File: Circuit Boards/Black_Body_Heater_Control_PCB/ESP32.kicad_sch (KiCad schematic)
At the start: 17 parts, among them J3 USB_C_Receptacle_USB2.0_14P, J4 Conn_01x04_Pin, SW1 430471035826, SW2 430471035826, U1 ESP32-S3-WROOM-1-N8R8, U4 USBLC6-2SC6

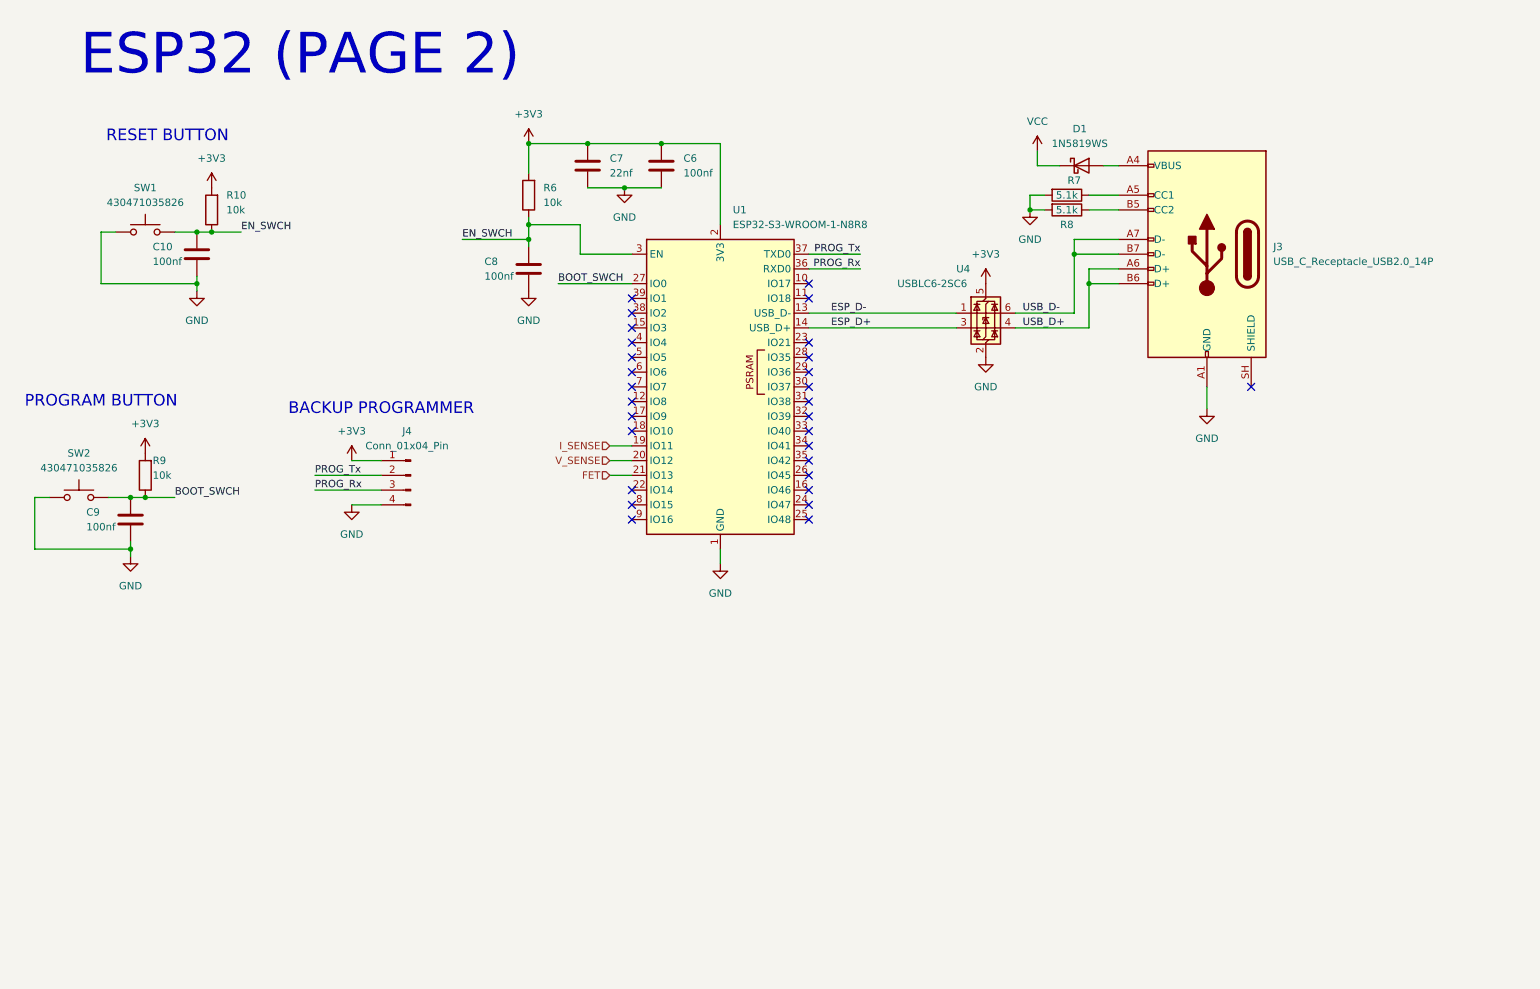
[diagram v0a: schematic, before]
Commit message: Heater PCB done (to review)
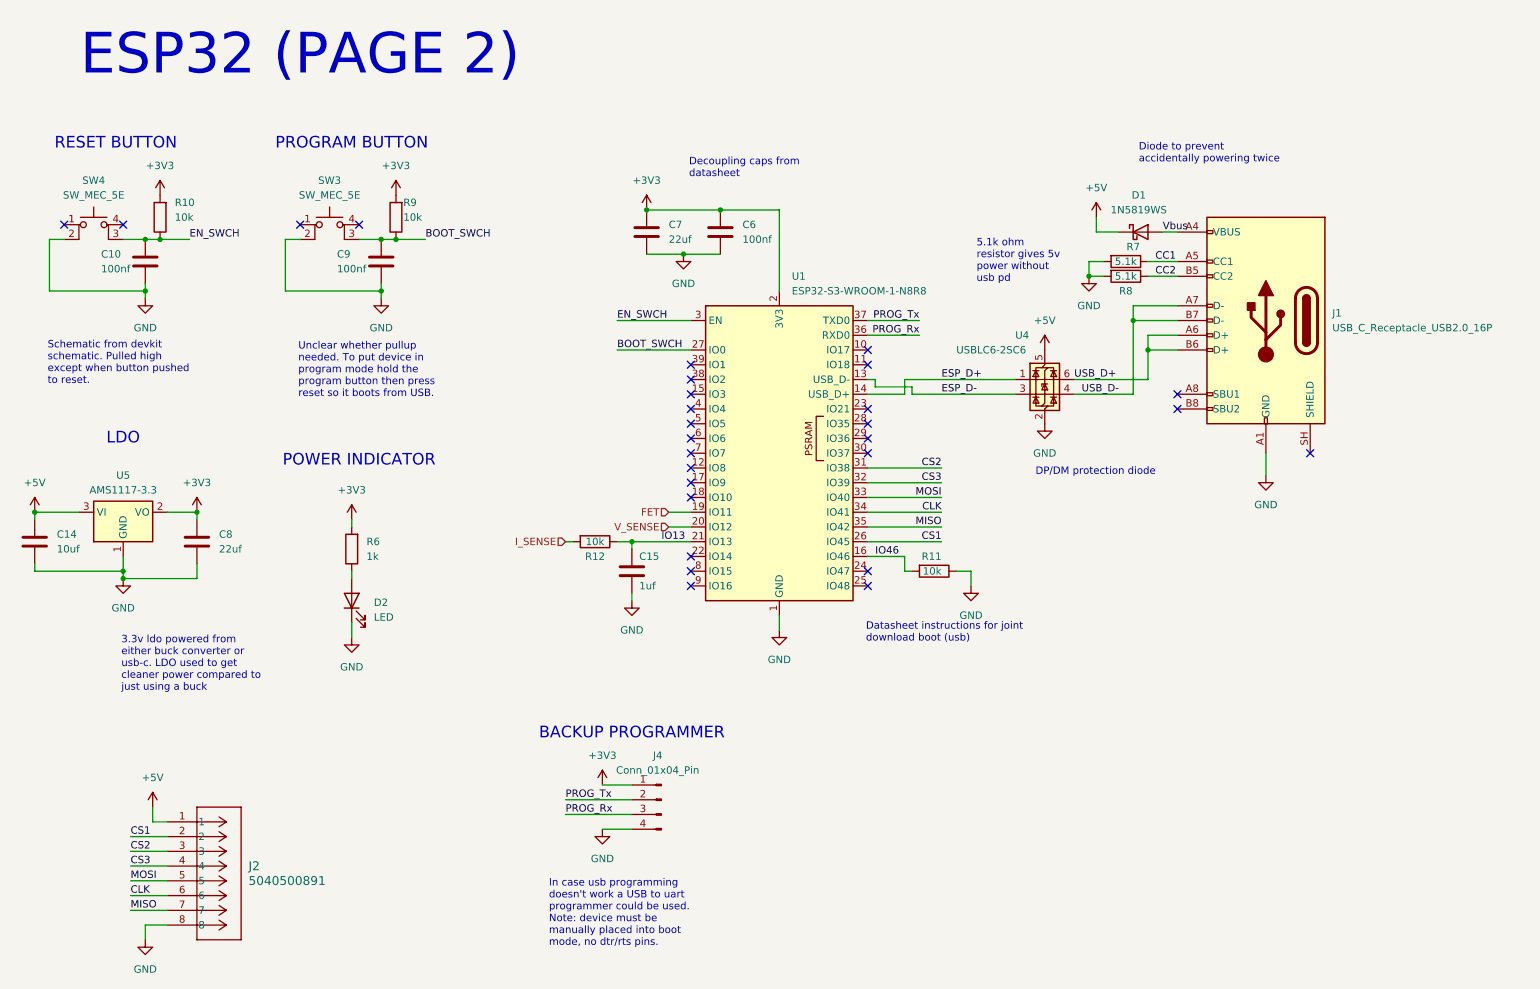
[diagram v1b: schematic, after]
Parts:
- removed J3: USB_C_Receptacle_USB2.0_14P, symbol Connector:USB_C_Receptacle_USB2.0_14P
- removed SW1, SW2: 430471035826, -switch:430471035826, symbol -switch:SW_Push
- added C14: 10uf, Capacitor_SMD:C_0603_1608Metric, symbol Device:C
- added C15: 1uf, Capacitor_SMD:C_0603_1608Metric, symbol Device:C
- added D2: LED, LED_SMD:LED_0603_1608Metric, symbol Device:LED
- added J1: USB_C_Receptacle_USB2.0_16P, -connector:UJ20-C-H-G-SMT-1-P16-TR, symbol Connector:USB_C_Receptacle_USB2.0_16P
- added J2: 5040500891, -connector:CONN_5040500891_MOL, symbol -connector:5040500891
- added R11, R12: 10k, Resistor_SMD:R_0603_1608Metric, symbol Device:R
- added SW3, SW4: SW_MEC_5E, -switch:430471035826, symbol Switch:SW_MEC_5E
- added U5: AMS1117-3.3, Package_TO_SOT_SMD:SOT-223-3_TabPin2, symbol Regulator_Linear:AMS1117-3.3
- C10, C6, C9: footprint (none) -> Capacitor_SMD:C_0603_1608Metric
- C7: value 22nf -> 22uf; footprint (none) -> Capacitor_SMD:C_0603_1608Metric
- C8: value 100nf -> 22uf; footprint (none) -> Capacitor_SMD:C_0603_1608Metric
- R10, R7, R8, R9: footprint (none) -> Resistor_SMD:R_0603_1608Metric
- R6: value 10k -> 1k; footprint (none) -> Resistor_SMD:R_0603_1608Metric
- U1: footprint RF_Module:ESP32-S3-WROOM-1 -> -mcu:ESP32-S3-WROOM-1
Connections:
- net +3V3: now also C8.1, U5.2 (VO); no longer U4.5 (VBUS)
- net BOOT_SWCH: now also SW3.3 (K)
- net EN_SWCH: now also SW4.3 (K); no longer C8.1, R6.1
- net ESP_D+: now also U4.1 (I/O1); no longer U4.3 (I/O2)
- net ESP_D-: now also U4.3 (I/O2); no longer U4.1 (I/O1)
- net FET: now also U1.19 (IO11); no longer U1.21 (IO13)
- net GND: now also C14.2, C15.2, D2.1 (K), J1.A1 (GND), J1.A12 (GND), J1.B1 (GND), J1.B12 (GND), J2.8, R11.1, SW3.2, SW4.2, U5.1 (GND)
- net I_SENSE: now also R12.2; no longer U1.19 (IO11)
- net USB_D+: now also U4.6 (I/O1), J1.A6 (D+), J1.B6 (D+); no longer U4.4 (I/O2)
- net USB_D-: now also U4.4 (I/O2), J1.A7 (D-), J1.B7 (D-); no longer U4.6 (I/O1)
- net Vbus: now reaches D1.2 (A)
- net Vbus: now also J1.A4 (VBUS), J1.A9 (VBUS), J1.B4 (VBUS), J1.B9 (VBUS)
- net IO46: now reaches U1.16 (IO46)
- net IO46: now also R11.2
- net CS1: now reaches U1.26 (IO45)
- net CS1: now also J2.2
- net CS2: now reaches U1.31 (IO38)
- net CS2: now also J2.3
- net CS3: now reaches U1.32 (IO39)
- net CS3: now also J2.4
- net MOSI: now reaches U1.33 (IO40)
- net MOSI: now also J2.5
- net CLK: now reaches U1.34 (IO41)
- net CLK: now also J2.6
- net MISO: now reaches U1.35 (IO42)
- net MISO: now also J2.7
- net CC1: now reaches R7.1
- net CC1: now also J1.A5 (CC1)
- net CC2: now reaches R8.1
- net CC2: now also J1.B5 (CC2)
- net VCC renamed +5V
- net +5V: now also U4.5 (VBUS), C14.1, J2.1, U5.3 (VI)
- new net: D2.2 (A), R6.1
- new net IO13: C15.1, R12.1, U1.21 (IO13)
- no-connect marks 29 -> 28
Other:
- note added: "LDO"
- note added: "POWER INDICATOR"
- moved on the sheet: C10, C6, C7, C9, D1, J4, R10, R7, R8, R9, U1

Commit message: Temp sensor schematic done
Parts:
- D2: value LED -> RED
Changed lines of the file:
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@@
 			)
 		)
-		(property "Value" "LED"
+		(property "Value" "RED"
 			(at 90.17 123.5074 90)
 			(show_name no)

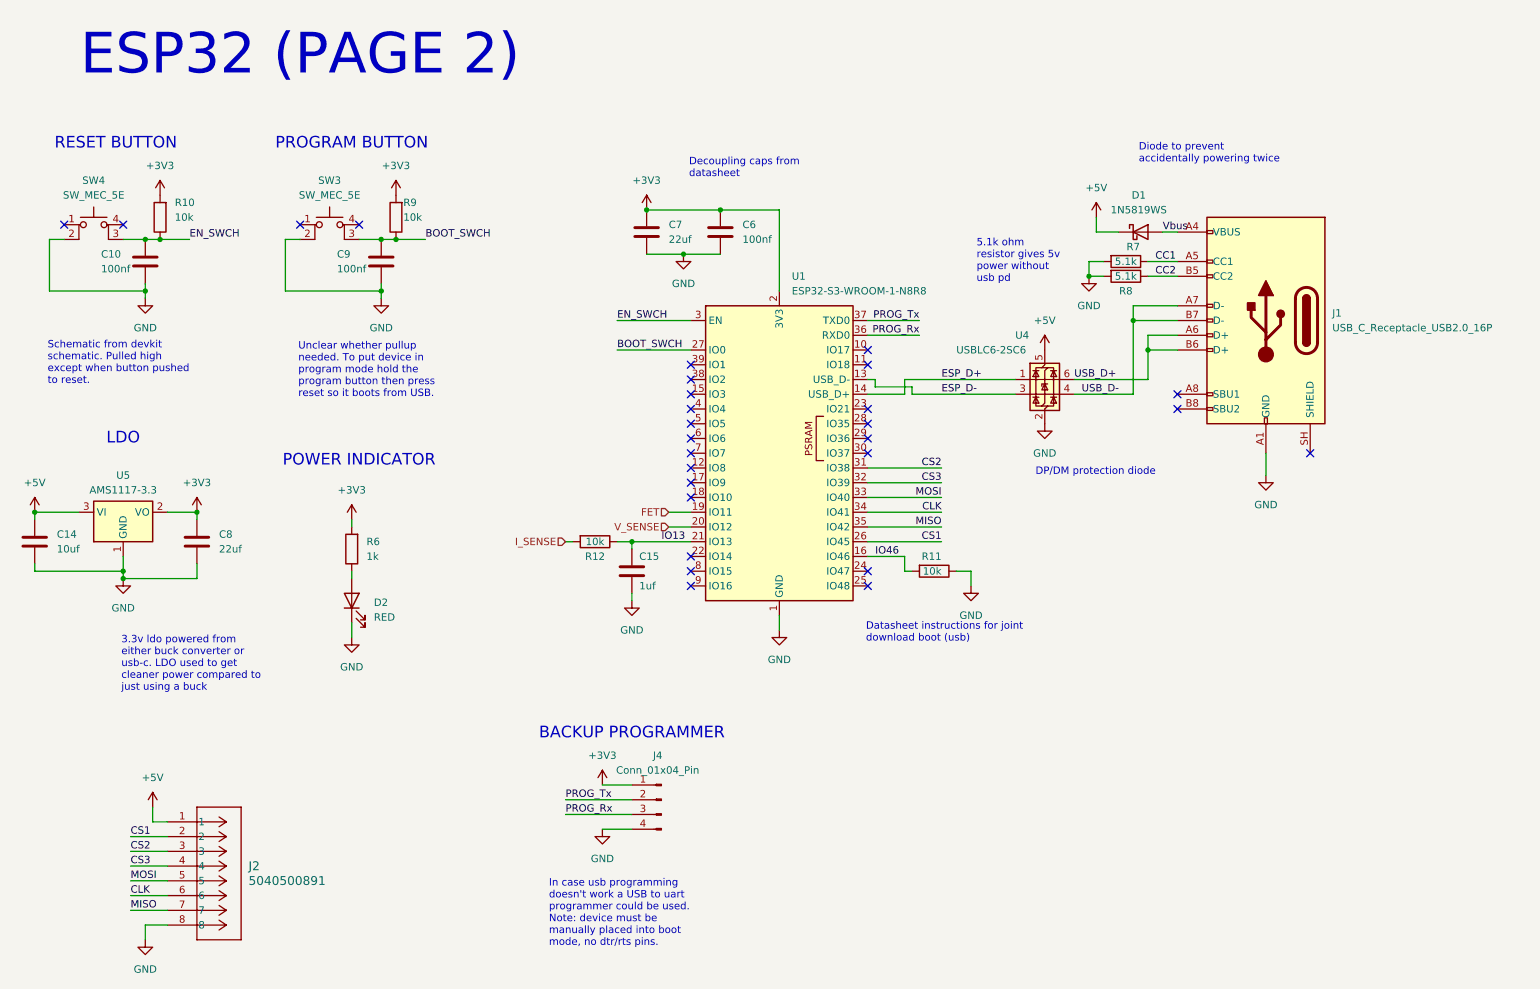
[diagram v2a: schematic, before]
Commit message: Heater switched from pwm to vccs
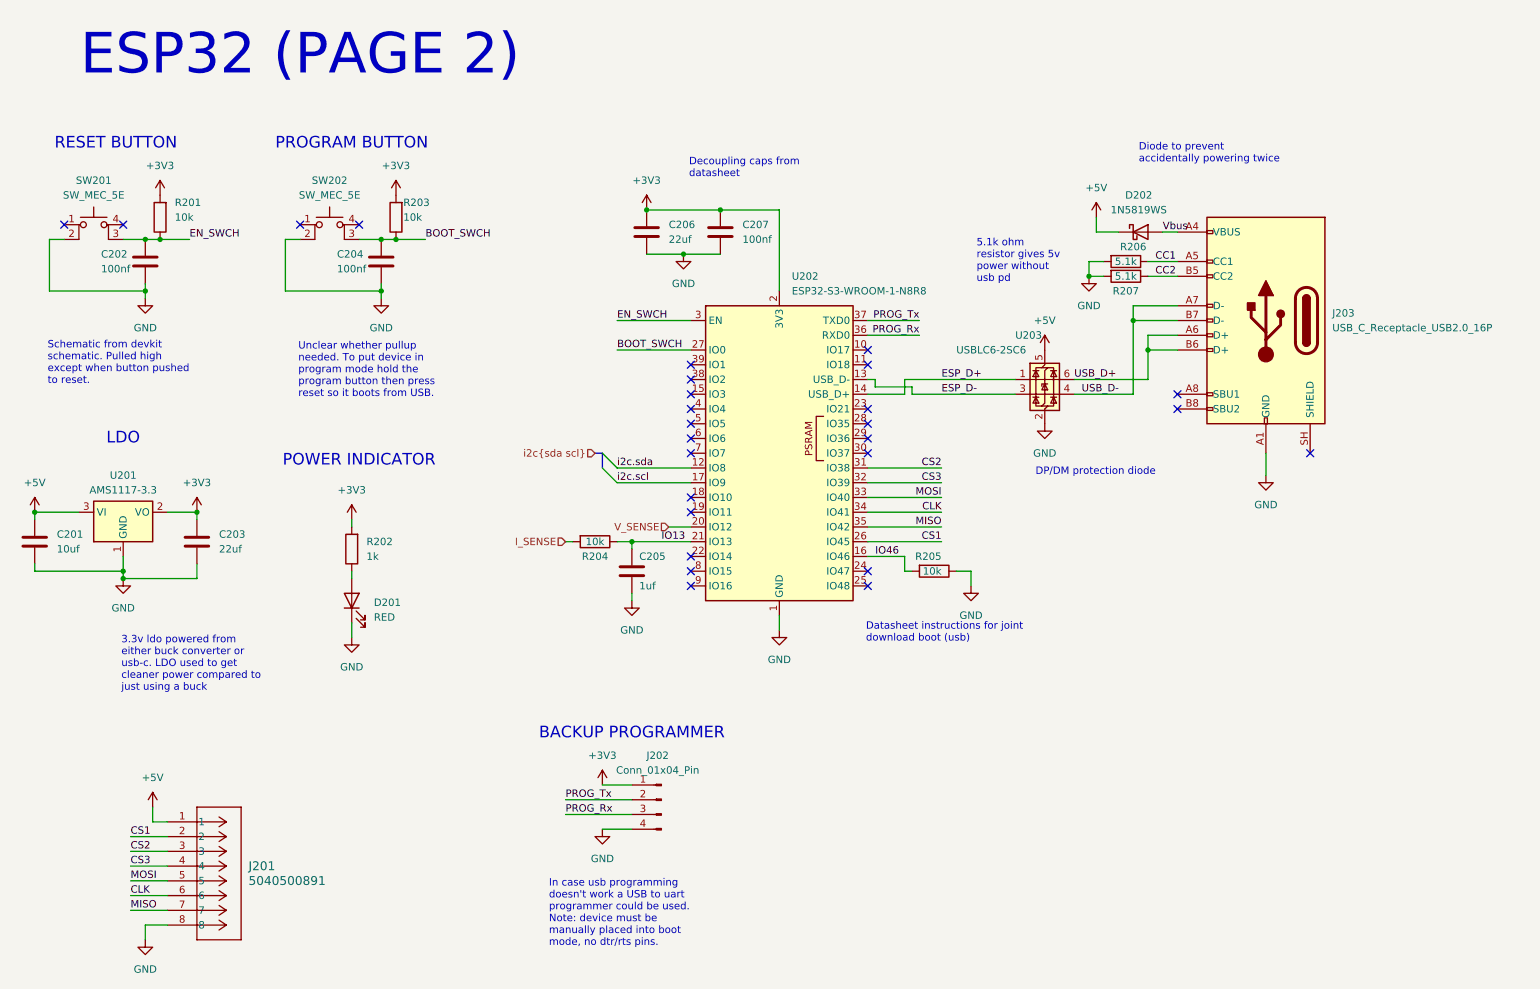
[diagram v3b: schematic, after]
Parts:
- renumbered C14 to C201, C10 to C202, C8 to C203, C9 to C204, C15 to C205, C7 to C206, C6 to C207, D2 to D201, D1 to D202, J2 to J201, J4 to J202, J1 to J203, R10 to R201, R6 to R202, R9 to R203, R12 to R204, R11 to R205, R7 to R206, R8 to R207, SW4 to SW201, SW3 to SW202, U5 to U201, U1 to U202, U4 to U203
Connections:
- net i2c.sda: now reaches U202.12 (IO8)
- net i2c.scl: now reaches U202.17 (IO9)
- net FET: no longer names the net of U202.19 (IO11)
- no-connect marks 28 -> 27

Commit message: heater ready to order
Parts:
- D202: MPN (none) -> 1N5819WS
- J201: MPN (none) -> 5040500891
- J202: now not fitted; now left out of the parts list
- J203: MPN (none) -> UJ20-C-H-G-SMT-1-P16-TR
- SW201, SW202: MPN (none) -> SW_MEC_5E
- U201: MPN (none) -> AMS1117-3.3
- U202: MPN (none) -> ESP32-S3-WROOM-1-N8R8
- U203: MPN (none) -> USBLC6-2SC6
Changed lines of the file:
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@@
 			)
 		)
+		(property "MPN" "SW_MEC_5E"
+			(at 41.91 58.42 0)
+			(hide yes)
+			(show_name no)
+			(do_not_autoplace no)
+			(effects
+				(font
+					(size 1.27 1.27)
+				)
+			)
+		)
 		(pin "4"
 		)
@@
 			)
 		)
+		(property "MPN" "USBLC6-2SC6"
+			(at 205.74 82.55 0)
+			(hide yes)
+			(show_name no)
+			(do_not_autoplace no)
+			(effects
+				(font
+					(size 1.27 1.27)
+				)
+			)
+		)
 		(pin "4"
 		)
@@
 	)
 	(symbol
+		(lib_id "Switch:SW_MEC_5E")
+		(at 82.55 58.42 0)
+		(unit 1)
+		(body_style 1)
+		(exclude_from_sim no)
+		(in_bom yes)
+		(on_board yes)
+		(in_pos_files yes)
+		(dnp no)
+		(fields_autoplaced yes)
+		(property "Reference" "SW202"
+			(at 82.55 48.26 0)
+			(show_name no)
+			(do_not_autoplace no)
+			(effects
+				(font
+					(size 1.27 1.27)
+				)
+			)
+		)
+		(property "Value" "SW_MEC_5E"
+			(at 82.55 50.8 0)
+			(show_name no)
+			(do_not_autoplace no)
+			(effects
+				(font
+					(size 1.27 1.27)
+				)
+			)
+		)
+		(property "Footprint" "-switch:430471035826"
+			(at 82.55 50.8 0)
+			(hide yes)
+			(show_name no)
+			(do_not_autoplace no)
+			(effects
+				(font
+					(size 1.27 1.27)
+				)
+			)
+		)
+		(property "Datasheet" "https://www.apem.com/medias/download/MEC_switches_serie_MULTIMEC5E.pdf"
+			(at 82.55 50.8 0)
+			(hide yes)
+			(show_name no)
+			(do_not_autoplace no)
+			(effects
+				(font
+					(size 1.27 1.27)
+				)
+			)
+		)
+		(property "Description" "MEC 5E single pole normally-open tactile switch"
+			(at 82.55 58.42 0)
+			(hide yes)
+			(show_name no)
+			(do_not_autoplace no)
+			(effects
+				(font
+					(size 1.27 1.27)
+				)
+			)
+		)
+		(property "MPN" "SW_MEC_5E"
+			(at 82.55 58.42 0)
+			(hide yes)
+			(show_name no)
+			(do_not_autoplace no)
+			(effects
+				(font
+					(size 1.27 1.27)
+				)
+			)
+		)
+		(pin "4"
+		)
+		(pin "3"
+		)
+		(pin "2"
+		)
+		(pin "1"
+		)
+		(instances
+			(project "Black_Body_Heater_Control"
+				(path "/f3dd8e24-b1a1-45ed-a541-b7ae36b7e8e0/81e90e05-0519-429e-85ab-ffede3727917"
+					(reference "SW202")
+					(unit 1)
+				)
+			)
+		)
+	)
+	(symbol
 		(lib_id "Diode:1N5819WS")
 		(at 222.25 57.15 0)
@@
 			)
 		)
+		(property "MPN" "1N5819WS"
+			(at 222.25 57.15 0)
+			(hide yes)
+			(show_name no)
+			(do_not_autoplace no)
+			(effects
+				(font
+					(size 1.27 1.27)
+				)
+			)
+		)
 		(pin "1"
 		)
@@
 			)
 		)
+		(property "MPN" "ESP32-S3-WROOM-1-N8R8"
+			(at 160.02 95.25 0)
+			(hide yes)
+			(show_name no)
+			(do_not_autoplace no)
+			(effects
+				(font
+					(size 1.27 1.27)
+				)
+			)
+		)
 		(pin "1"
 		)
@@
 			)
 		)
+		(property "MPN" "UJ20-C-H-G-SMT-1-P16-TR"
+			(at 243.84 72.39 0)
+			(hide yes)
+			(show_name no)
+			(do_not_autoplace no)
+			(effects
+				(font
+					(size 1.27 1.27)
+				)
+			)
+		)
 		(pin "A4"
 		)
@@
 			)
 		)
+		(property "MPN" "5040500891"
+			(at 54.61 158.75 0)
+			(hide yes)
+			(show_name yes)
+			(do_not_autoplace no)
+			(effects
+				(font
+					(size 1.27 1.27)
+				)
+				(justify bottom)
+			)
+		)
 		(pin "4"
 		)
@@
 	)
 	(symbol
-		(lib_id "Switch:SW_MEC_5E")
-		(at 82.55 58.42 0)
-		(unit 1)
-		(body_style 1)
-		(exclude_from_sim no)
-		(in_bom yes)
-		(on_board yes)
-		(in_pos_files yes)
-		(dnp no)
-		(fields_autoplaced yes)
-		(property "Reference" "SW202"
-			(at 82.55 48.26 0)
-			(show_name no)
-			(do_not_autoplace no)
-			(effects
-				(font
-					(size 1.27 1.27)
-				)
-			)
-		)
-		(property "Value" "SW_MEC_5E"
-			(at 82.55 50.8 0)
-			(show_name no)
-			(do_not_autoplace no)
-			(effects
-				(font
-					(size 1.27 1.27)
-				)
-			)
-		)
-		(property "Footprint" "-switch:430471035826"
-			(at 82.55 50.8 0)
-			(hide yes)
-			(show_name no)
-			(do_not_autoplace no)
-			(effects
-				(font
-					(size 1.27 1.27)
-				)
-			)
-		)
-		(property "Datasheet" "https://www.apem.com/medias/download/MEC_switches_serie_MULTIMEC5E.pdf"
-			(at 82.55 50.8 0)
-			(hide yes)
-			(show_name no)
-			(do_not_autoplace no)
-			(effects
-				(font
-					(size 1.27 1.27)
-				)
-			)
-		)
-		(property "Description" "MEC 5E single pole normally-open tactile switch"
-			(at 82.55 58.42 0)
-			(hide yes)
-			(show_name no)
-			(do_not_autoplace no)
-			(effects
-				(font
-					(size 1.27 1.27)
-				)
-			)
-		)
-		(pin "4"
-		)
-		(pin "3"
-		)
-		(pin "2"
-		)
-		(pin "1"
-		)
-		(instances
-			(project "Black_Body_Heater_Control"
-				(path "/f3dd8e24-b1a1-45ed-a541-b7ae36b7e8e0/81e90e05-0519-429e-85ab-ffede3727917"
-					(reference "SW202")
-					(unit 1)
-				)
-			)
-		)
-	)
-	(symbol
 		(lib_id "power:+3V3")
 		(at 86.36 106.68 0)
@@
 		(body_style 1)
 		(exclude_from_sim no)
-		(in_bom yes)
+		(in_bom no)
 		(on_board yes)
 		(in_pos_files yes)
-		(dnp no)
+		(dnp yes)
 		(property "Reference" "J202"
 			(at 139.065 147.32 0)
@@
 			(at 46.99 105.41 0)
 			(hide yes)
+			(show_name no)
+			(do_not_autoplace no)
+			(effects
+				(font
+					(size 1.27 1.27)
+				)
+			)
+		)
+		(property "MPN" "AMS1117-3.3"
+			(at 46.99 105.41 0)
+			(hide yes)
